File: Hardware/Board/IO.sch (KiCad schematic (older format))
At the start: 175 parts, among them IC200 BTS6143D, IC201 BTS6143D, IC203 BTS6143D, IC204 BTS6143D, Q200 2N7002, Q201 2N7002, Q202 2N7002, Q203 2N7002, U200 SN74LV4052A, U201 TJA1029T, U202 TJA1029T, U203 TJA1029T, U204 TJA1029T, U205 SN74LV4052A, U206 SN74LV4052A, U207 MAX3072E, U208 MAX3072E, U209 MAX3072E, U210 MAX3072E, U211 MAX11615, U212 PCF8574A, U213 TJA1049T-3, U214 DS2482S-800+, U215 SI8422BB-D-IS, U215 SN74LV4052A, U216 SI8422BB-D-IS, U217 SI8422BB-D-IS, U218 SI8422BB-D-IS, U219 USBLC6-2SC6, U220 USBLC6-2SC6, U221 USBLC6-2SC6, U222 USBLC6-2SC6

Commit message: Board: Änderung Footprints, Debug geroutet, Beginn Platzierung Netzteil, Bezeichnungen und Werte aufgeräumt.
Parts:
- removed C218: 100nF, Capacitor_SMD:C_0603_1608Metric, symbol Womo-rescue:C-Device
- removed U213: TJA1049T-3, Package_SO:SOIC-8_3.9x4.9mm_P1.27mm, symbol Womo-rescue:TJA1049T-3-Interface_CAN_LIN
- added R253: 47k, Resistor_SMD:R_0603_1608Metric, symbol Womo-rescue:R-Device
- added U213: SN65HVD234, Package_SO:SOIC-8_3.9x4.9mm_P1.27mm, symbol Interface_CAN_LIN:SN65HVD234
- C200, C201, C203, C205, C207, C209, C210, C211, C212, C213, C214, C215, C216, C217, C221, C222: value 100nF -> 100n
- C202, C204, C206, C208: value 220pF -> 220p
- C220: value 10uF -> 1u; footprint Capacitor_SMD:C_1210_3225Metric -> Capacitor_SMD:C_1206_3216Metric
- C231, C232, C233, C234: value 47u -> 10u
- R200, R228, R229: value 10K -> 10k
- R201: value 1K -> 1k
- renumbered IC200 to U224, IC201 to U225, IC203 to U226, IC204 to U227
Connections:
- net labels removed: +5V
- wire segments 627 -> 625

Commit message: Board: PSU platziert, Fehlerkorrektur, Routing PSU
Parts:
- D221, D222: footprint Diode_SMD:D_SMB -> Diode_SMD:D_SMC
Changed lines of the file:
@@
 F 0 "D221" V 19100 1950 50  0000 C CNN
 F 1 "B345BE-13" V 19000 1800 50  0000 C CNN
-F 2 "Diode_SMD:D_SMB" H 18600 1800 50  0001 C CNN
+F 2 "Diode_SMD:D_SMC" H 18600 1800 50  0001 C CNN
 F 3 "~" H 18600 1800 50  0001 C CNN
 	1    18600 1800
@@
 F 0 "D222" V 19400 1750 50  0000 C CNN
 F 1 "B345BE-13" V 19300 1600 50  0000 C CNN
-F 2 "Diode_SMD:D_SMB" H 18900 1800 50  0001 C CNN
+F 2 "Diode_SMD:D_SMC" H 18900 1800 50  0001 C CNN
 F 3 "~" H 18900 1800 50  0001 C CNN
 	1    18900 1800

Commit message: Board: Power LED hinzu gefügt, Layout 99% fertig
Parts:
- removed D221, D222: B345BE-13, Diode_SMD:D_SMC, symbol Womo-rescue:DIODE-pspice
- added D221, D222: B560C, Diode_SMD:D_SMC, symbol Diode:B260
- R202, R204, R206: value 10K -> 10k
- R203, R205, R207: value 1K -> 1k
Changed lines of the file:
@@
 P 6850 3750
 F 0 "R203" H 6920 3796 50  0000 L CNN
-F 1 "1K" H 6920 3705 50  0000 L CNN
+F 1 "1k" H 6920 3705 50  0000 L CNN
 F 2 "Resistor_SMD:R_0603_1608Metric" V 6780 3750 50  0001 C CNN
 F 3 "~" H 6850 3750 50  0001 C CNN
@@
 P 6850 5550
 F 0 "R205" H 6920 5596 50  0000 L CNN
-F 1 "1K" H 6920 5505 50  0000 L CNN
+F 1 "1k" H 6920 5505 50  0000 L CNN
 F 2 "Resistor_SMD:R_0603_1608Metric" V 6780 5550 50  0001 C CNN
 F 3 "~" H 6850 5550 50  0001 C CNN
@@
 P 5150 3300
 F 0 "R202" H 5220 3346 50  0000 L CNN
-F 1 "10K" H 5220 3255 50  0000 L CNN
+F 1 "10k" H 5220 3255 50  0000 L CNN
 F 2 "Resistor_SMD:R_0603_1608Metric" V 5080 3300 50  0001 C CNN
 F 3 "~" H 5150 3300 50  0001 C CNN
@@
 P 5150 5150
 F 0 "R204" H 5220 5196 50  0000 L CNN
-F 1 "10K" H 5220 5105 50  0000 L CNN
+F 1 "10k" H 5220 5105 50  0000 L CNN
 F 2 "Resistor_SMD:R_0603_1608Metric" V 5080 5150 50  0001 C CNN
 F 3 "~" H 5150 5150 50  0001 C CNN
@@
 P 6850 7500
 F 0 "R207" H 6920 7546 50  0000 L CNN
-F 1 "1K" H 6920 7455 50  0000 L CNN
+F 1 "1k" H 6920 7455 50  0000 L CNN
 F 2 "Resistor_SMD:R_0603_1608Metric" V 6780 7500 50  0001 C CNN
 F 3 "~" H 6850 7500 50  0001 C CNN
@@
 P 5150 7100
 F 0 "R206" H 5220 7146 50  0000 L CNN
-F 1 "10K" H 5220 7055 50  0000 L CNN
+F 1 "10k" H 5220 7055 50  0000 L CNN
 F 2 "Resistor_SMD:R_0603_1608Metric" V 5080 7100 50  0001 C CNN
 F 3 "~" H 5150 7100 50  0001 C CNN
@@
 Text GLabel 17900 1600 0    50   Input ~ 0
 DC_Input
-$Comp
-L Womo-rescue:DIODE-pspice D?
-U 1 1 5E3DC596
-P 18600 1800
-AR Path="/5C8BBC9A/5E3DC596" Ref="D?"  Part="1"
-AR Path="/5E0C5EEA/5E3DC596" Ref="D?"  Part="1"
-AR Path="/5C8BBC97/5E3DC596" Ref="D221"  Part="1"
-F 0 "D221" V 19100 1950 50  0000 C CNN
-F 1 "B345BE-13" V 19000 1800 50  0000 C CNN
-F 2 "Diode_SMD:D_SMC" H 18600 1800 50  0001 C CNN
-F 3 "~" H 18600 1800 50  0001 C CNN
-	1    18600 1800
-	0    -1   -1   0
-$EndComp
-$Comp
-L Womo-rescue:DIODE-pspice D?
-U 1 1 5E3DC59D
-P 18900 1800
-AR Path="/5C8BBC9A/5E3DC59D" Ref="D?"  Part="1"
-AR Path="/5E0C5EEA/5E3DC59D" Ref="D?"  Part="1"
-AR Path="/5C8BBC97/5E3DC59D" Ref="D222"  Part="1"
-F 0 "D222" V 19400 1750 50  0000 C CNN
-F 1 "B345BE-13" V 19300 1600 50  0000 C CNN
-F 2 "Diode_SMD:D_SMC" H 18900 1800 50  0001 C CNN
-F 3 "~" H 18900 1800 50  0001 C CNN
-	1    18900 1800
-	0    -1   -1   0
-$EndComp
-$Comp
-L Womo-rescue:GND-power #PWR?
-U 1 1 5E3DC5A4
-P 18600 2000
-AR Path="/5C8BBC9A/5E3DC5A4" Ref="#PWR?"  Part="1"
-AR Path="/5E0C5EEA/5E3DC5A4" Ref="#PWR?"  Part="1"
-AR Path="/5C8BBC97/5E3DC5A4" Ref="#PWR0476"  Part="1"
-F 0 "#PWR0476" H 18600 1750 50  0001 C CNN
-F 1 "GND" H 18605 1827 50  0000 C CNN
-F 2 "" H 18600 2000 50  0001 C CNN
-F 3 "" H 18600 2000 50  0001 C CNN
-	1    18600 2000
-	1    0    0    -1
-$EndComp
-$Comp
-L Womo-rescue:GND-power #PWR?
-U 1 1 5E3DC5AA
-P 18900 2000
-AR Path="/5C8BBC9A/5E3DC5AA" Ref="#PWR?"  Part="1"
-AR Path="/5E0C5EEA/5E3DC5AA" Ref="#PWR?"  Part="1"
-AR Path="/5C8BBC97/5E3DC5AA" Ref="#PWR0477"  Part="1"
-F 0 "#PWR0477" H 18900 1750 50  0001 C CNN
-F 1 "GND" H 18905 1827 50  0000 C CNN
-F 2 "" H 18900 2000 50  0001 C CNN
-F 3 "" H 18900 2000 50  0001 C CNN
-	1    18900 2000
-	1    0    0    -1
-$EndComp
-Wire Wire Line
-	18900 1600 18600 1600
-Connection ~ 18900 1600
-Wire Wire Line
-	18300 1600 18600 1600
-Connection ~ 18600 1600
 Wire Wire Line
 	17900 1600 18000 1600
@@
 Wire Wire Line
 	19300 3550 19300 2900
-Wire Wire Line
-	18900 1600 19300 1600
 Connection ~ 19300 1600
 Wire Wire Line
@@
 	1    0    0    -1
 $EndComp
+$Comp
+L Womo-rescue:GND-power #PWR?
+U 1 1 6656C530
+P 18600 1900
+AR Path="/5C8BBC9A/6656C530" Ref="#PWR?"  Part="1"
+AR Path="/5E0C5EEA/6656C530" Ref="#PWR?"  Part="1"
+AR Path="/5C8BBC97/6656C530" Ref="#PWR0420"  Part="1"
+F 0 "#PWR0420" H 18600 1650 50  0001 C CNN
+F 1 "GND" H 18605 1727 50  0000 C CNN
+F 2 "" H 18600 1900 50  0001 C CNN
+F 3 "" H 18600 1900 50  0001 C CNN
+	1    18600 1900
+	1    0    0    -1
+$EndComp
+$Comp
+L Womo-rescue:GND-power #PWR?
+U 1 1 6656C536
+P 18900 1900
+AR Path="/5C8BBC9A/6656C536" Ref="#PWR?"  Part="1"
+AR Path="/5E0C5EEA/6656C536" Ref="#PWR?"  Part="1"
+AR Path="/5C8BBC97/6656C536" Ref="#PWR0421"  Part="1"
+F 0 "#PWR0421" H 18900 1650 50  0001 C CNN
+F 1 "GND" H 18905 1727 50  0000 C CNN
+F 2 "" H 18900 1900 50  0001 C CNN
+F 3 "" H 18900 1900 50  0001 C CNN
+	1    18900 1900
+	1    0    0    -1
+$EndComp
+$Comp
+L Diode:B260 D?
+U 1 1 6656C53C
+P 18600 1750
+AR Path="/5C8BBC9A/6656C53C" Ref="D?"  Part="1"
+AR Path="/5C8BBC97/6656C53C" Ref="D221"  Part="1"
+F 0 "D221" V 18700 1400 50  0000 L CNN
+F 1 "B560C" V 18800 1400 50  0000 L CNN
+F 2 "Diode_SMD:D_SMC" H 18600 1575 50  0001 C CNN
+F 3 "http://www.jameco.com/Jameco/Products/ProdDS/1538777.pdf" H 18600 1750 50  0001 C CNN
+	1    18600 1750
+	0    1    1    0
+$EndComp
+$Comp
+L Diode:B260 D?
+U 1 1 6656C542
+P 18900 1750
+AR Path="/5C8BBC9A/6656C542" Ref="D?"  Part="1"
+AR Path="/5C8BBC97/6656C542" Ref="D222"  Part="1"
+F 0 "D222" V 19000 1850 50  0000 L CNN
+F 1 "B560C" V 19100 1850 50  0000 L CNN
+F 2 "Diode_SMD:D_SMC" H 18900 1575 50  0001 C CNN
+F 3 "http://www.jameco.com/Jameco/Products/ProdDS/1538777.pdf" H 18900 1750 50  0001 C CNN
+	1    18900 1750
+	0    1    1    0
+$EndComp
+Wire Wire Line
+	18300 1600 18600 1600
+Connection ~ 18600 1600
+Wire Wire Line
+	18600 1600 18900 1600
+Connection ~ 18900 1600
+Wire Wire Line
+	18900 1600 19300 1600
 $EndSCHEMATC

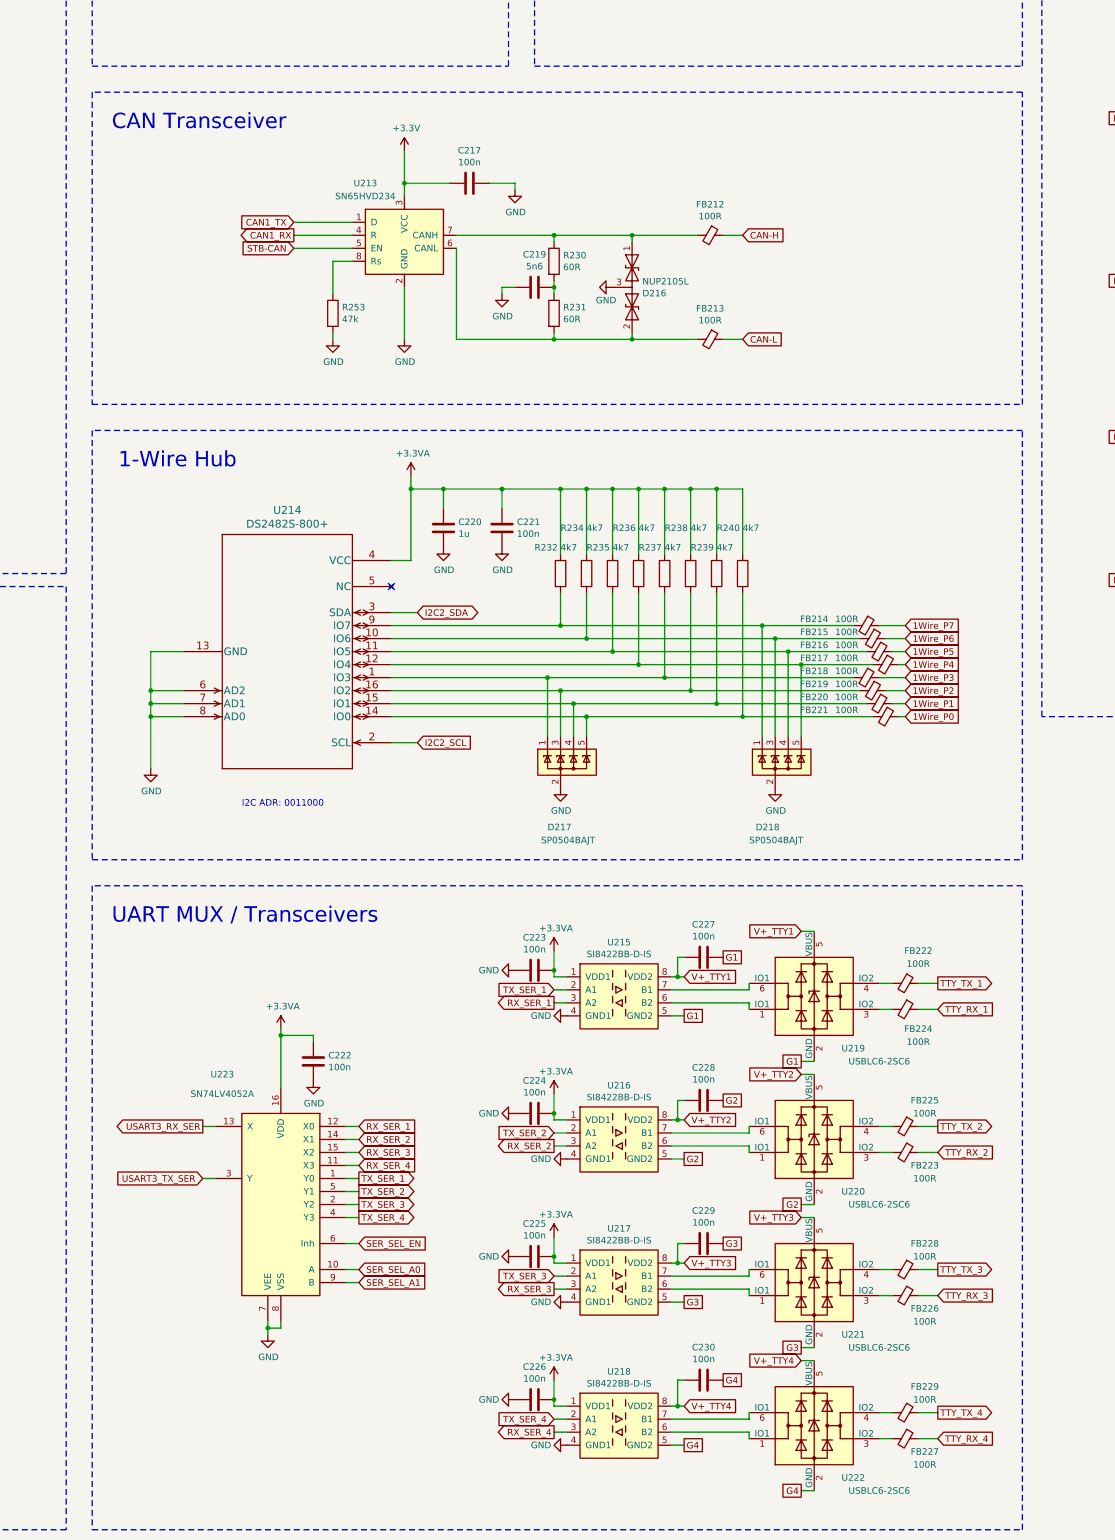
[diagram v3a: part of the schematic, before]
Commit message: Fix VE direct bug in schematic
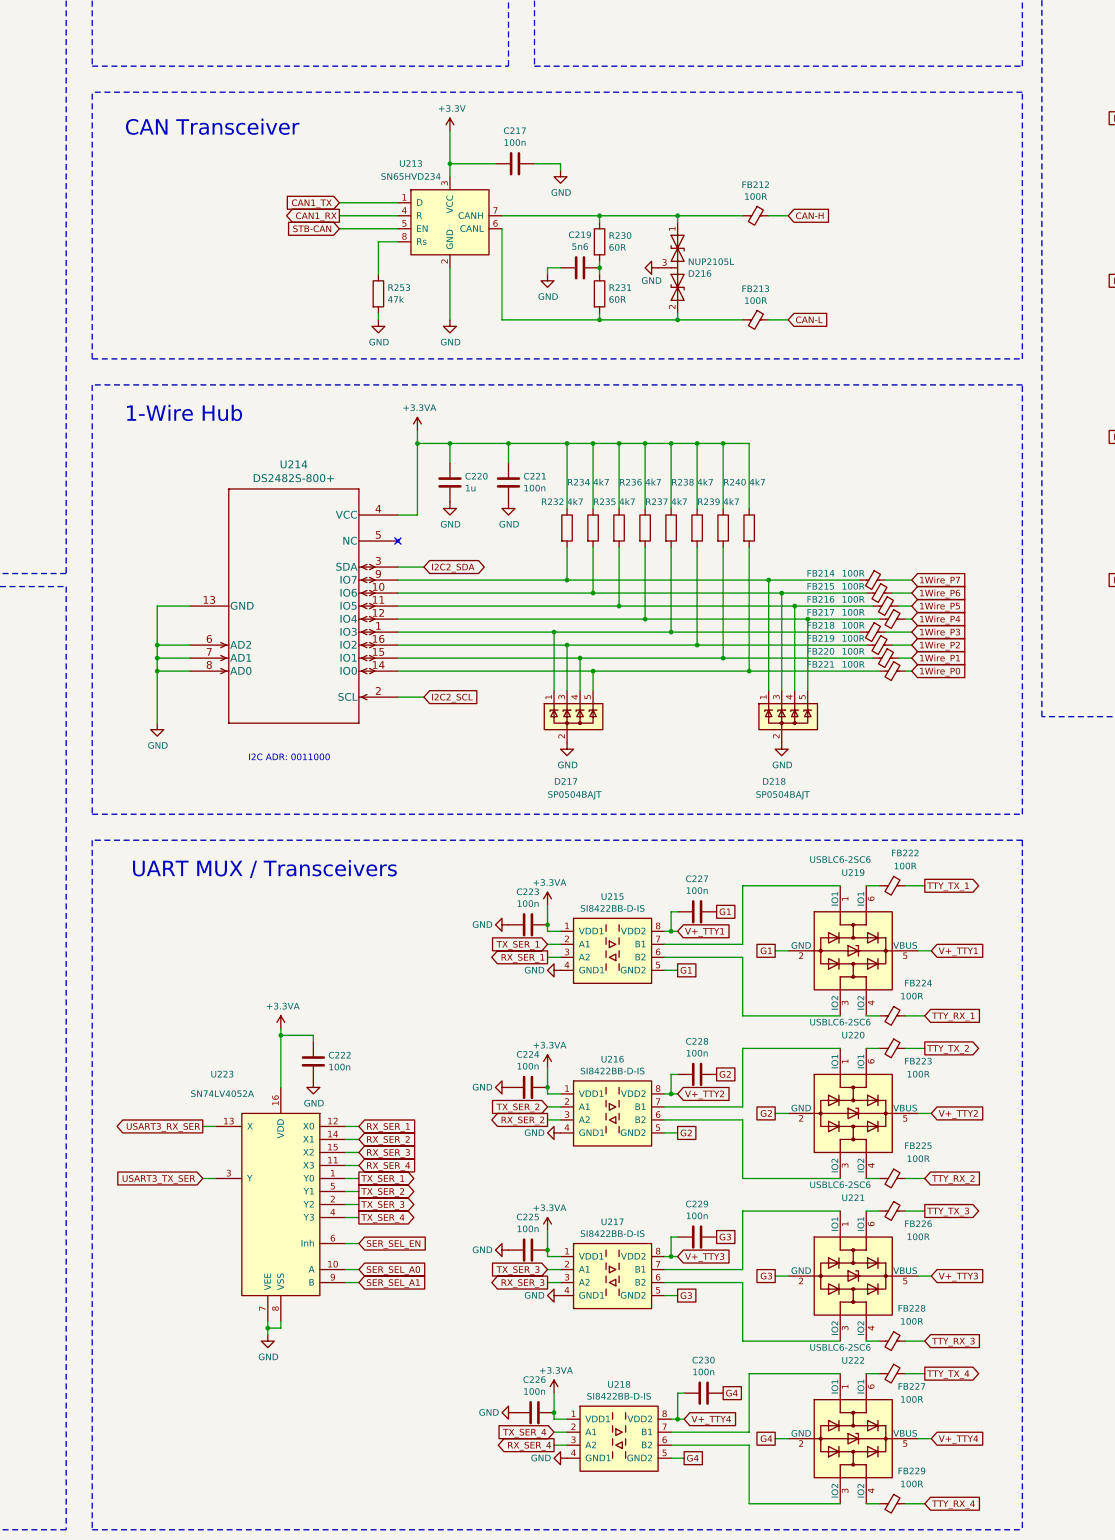
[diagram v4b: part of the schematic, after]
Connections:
- net at U215.6 (B2): now also U219.3 (IO2); no longer U219.1 (IO1)
- net at U215.7 (B1): now also U219.1 (IO1); no longer U219.6 (IO1)
- net at U217.6 (B2): now also U221.3 (IO2); no longer U221.1 (IO1)
- net at U217.7 (B1): now also U221.1 (IO1); no longer U221.6 (IO1)
- net at U216.6 (B2): now also U220.3 (IO2); no longer U220.1 (IO1)
- net at U216.7 (B1): now also U220.1 (IO1); no longer U220.6 (IO1)
- net at U218.6 (B2): now also U222.3 (IO2); no longer U222.1 (IO1)
- net at U218.7 (B1): now also U222.1 (IO1); no longer U222.6 (IO1)
- net at FB222.2: now also U219.6 (IO1); no longer U219.4 (IO2)
- net at FB223.2: now also U220.6 (IO1); no longer U220.4 (IO2)
- net at FB224.2: now also U219.4 (IO2); no longer U219.3 (IO2)
- net at FB225.2: now also U220.4 (IO2); no longer U220.3 (IO2)
- net at FB226.2: now also U221.6 (IO1); no longer U221.4 (IO2)
- net at FB227.2: now also U222.6 (IO1); no longer U222.4 (IO2)
- net at FB228.2: now also U221.4 (IO2); no longer U221.3 (IO2)
- net at FB229.2: now also U222.4 (IO2); no longer U222.3 (IO2)
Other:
- moved on the sheet: C217, C219, C220, C221, C223, C224, C225, C226, C227, C228, C229, C230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

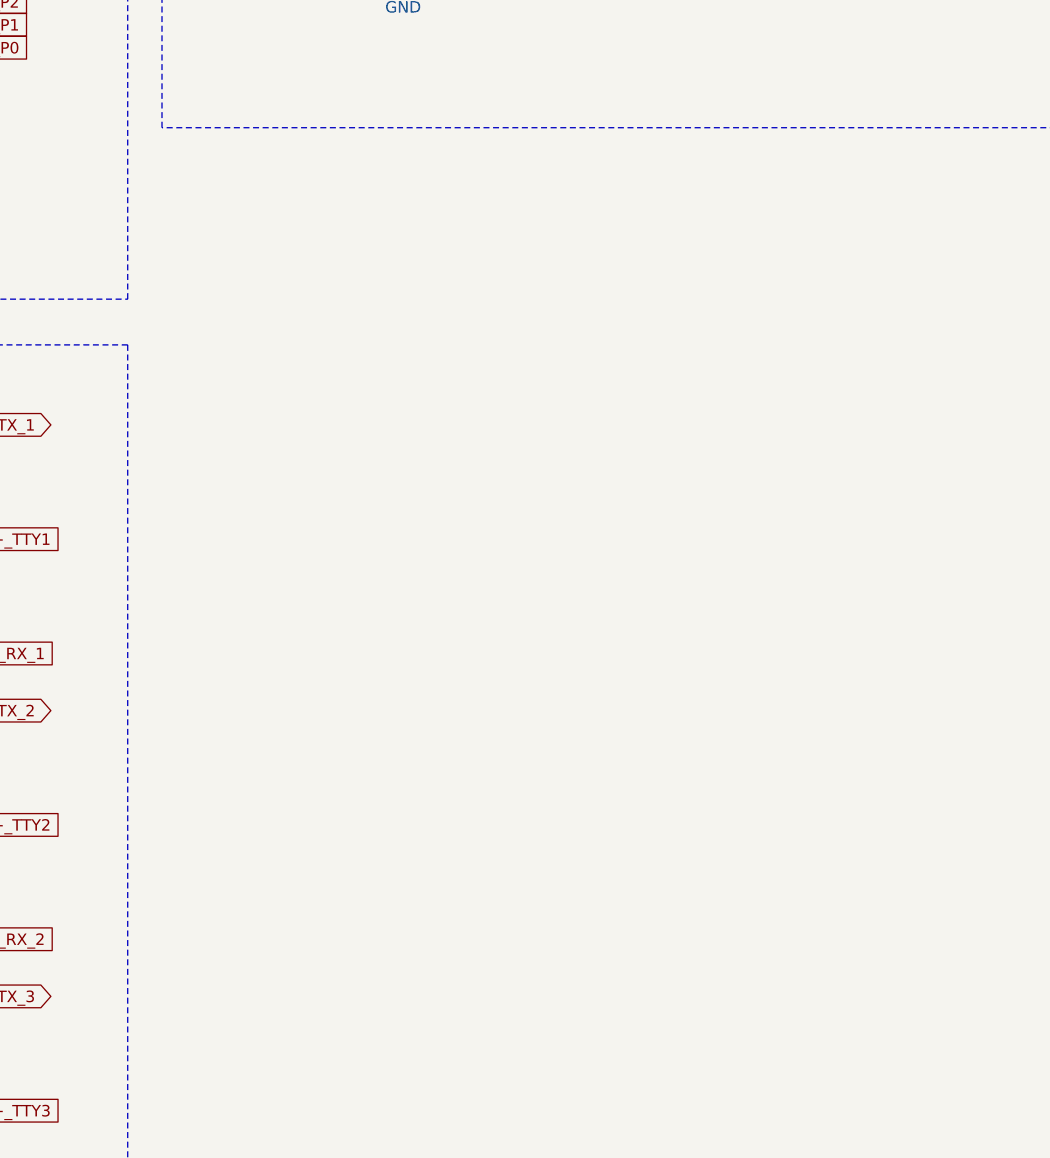
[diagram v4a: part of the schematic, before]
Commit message: Add CAN to ESP 32 and Raspberry (nicht fertig) diverse Fehlerkorrekturen.
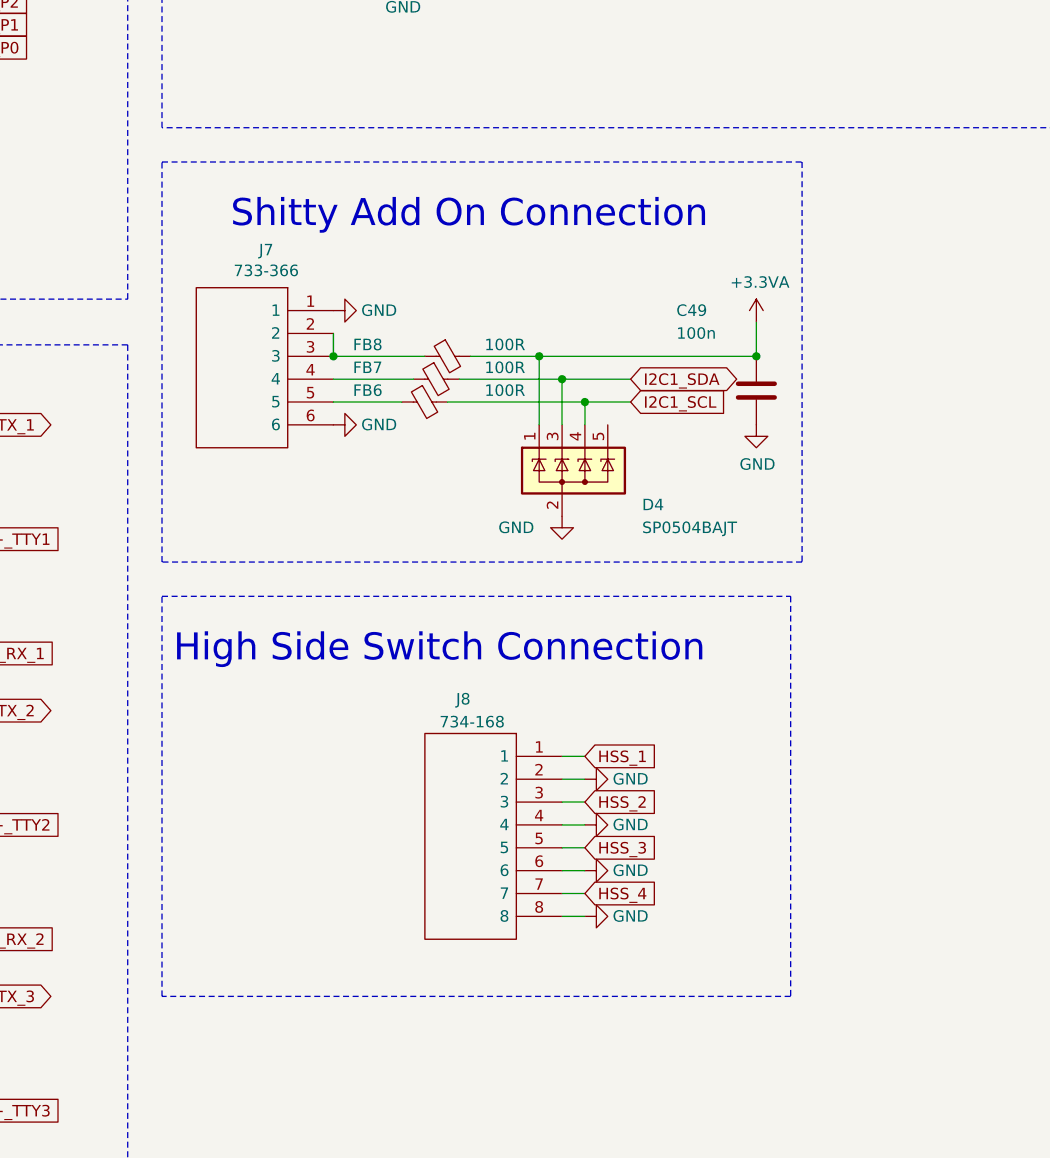
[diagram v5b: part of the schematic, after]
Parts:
- added C49: 100n, Capacitor_SMD:C_0603_1608Metric, symbol Womo-rescue:C-Device
- added D4: SP0504BAJT, Package_TO_SOT_SMD:SOT-353_SC-70-5, symbol Womo-rescue:SP0504BAJT-Power_Protection
- added FB6, FB7, FB8: 100R, Inductor_SMD:L_0603_1608Metric, symbol Womo-rescue:Ferrite_Bead_Small-Device
- added J7: 733-366, WAGO:SHDR6W80P0X250_1X6_1750X890X780P, symbol WAGO:733-366
- added J8: 734-168, WAGO:SHDR8W150P350X350_1X8_3040X1030X860P, symbol WAGO:734-168
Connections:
- net +3.3VA: now also C49.1, D4.1 (K), FB8.2
- net GND: now also C49.2, D4.2 (A), J7.1, J7.6, J8.2, J8.4, J8.6, J8.8
- net HSS_1: now also J8.1
- net HSS_2: now also J8.3
- net HSS_3: now also J8.5
- net HSS_4: now also J8.7
- new net: FB8.1, J7.2, J7.3
- new net: FB7.1, J7.4
- new net: FB6.1, J7.5
- new net I2C1_SCL: D4.4 (K), FB6.2
- new net I2C1_SDA: D4.3 (K), FB7.2
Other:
- note added: "High Side Switch Connection"
- note added: "Shitty Add On Connection"
